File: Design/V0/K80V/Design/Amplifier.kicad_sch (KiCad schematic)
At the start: 59 parts

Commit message: affectations des empreintes
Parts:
- C1, C10, C11, C12, C13, C14, C15, C16, C2, C3, C4, C5, C6, C9: renamed from C?; footprint Design:C_0805_2012Metric -> Capacitor_SMD:C_0805_2012Metric
- C7, C8: renamed from C?; footprint Design:C_1210_3225Metric -> Capacitor_SMD:C_1210_3225Metric
- R1, R10, R12, R13, R14, R15, R16, R17, R18, R19, R2, R3, R4, R5, R6, R7, R8: renamed from R?; footprint Design:R_MELF_MMB-0207 -> Resistor_SMD:R_MELF_MMB-0207
- R11, R20, R21, R22, R23, R24, R25, R9: renamed from R?; footprint Design:R_0805_2012Metric -> Resistor_SMD:R_0805_2012Metric
- U1, U2, U4: renamed from U?; footprint Design:SOIC-8_3.9x4.9mm_P1.27mm -> Package_SO:SOIC-8_3.9x4.9mm_P1.27mm
- U3: renamed from U?; footprint Design:SOT-23 -> Package_SO:TSOP-6_1.65x3.05mm_P0.95mm
- U5: renamed from U?; footprint (none) -> Package_SO:SOIC-8_3.9x4.9mm_P1.27mm
- U6: renamed from U?; footprint Design:AD5752AREZ -> baclet_composants_np:AD5752AREZ
- U7: renamed from U?; footprint Design:MSOP-8_3x3mm_P0.65mm -> Package_SO:MSOP-8_3x3mm_P0.65mm
- U8: renamed from U?; footprint Design:TSSOP-14_4.4x5mm_P0.65mm -> Package_SO:TSSOP-14_4.4x5mm_P0.65mm
- gave numbers to parts that had none: 2

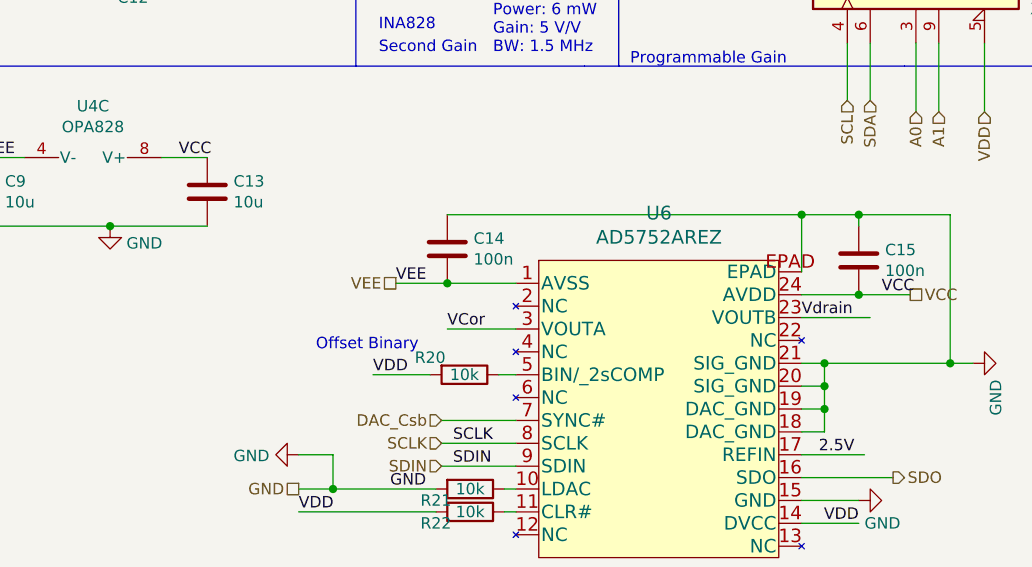
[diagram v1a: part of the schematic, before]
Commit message: Assignation des bons symboles
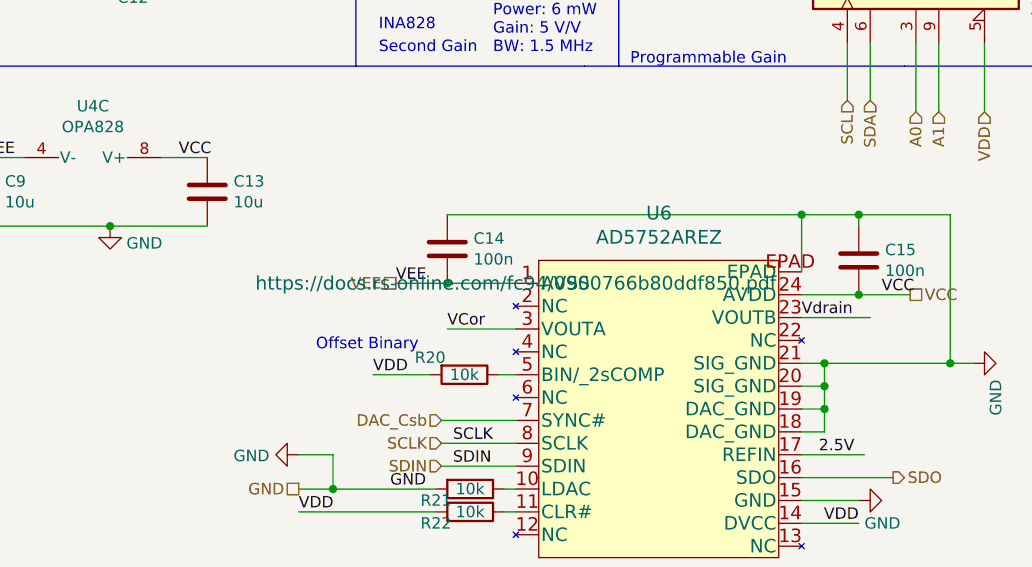
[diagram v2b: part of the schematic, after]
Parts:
- C1, C10, C11, C12, C13, C16, C2, C3, C4, C5, C6, C7, C8, C9: symbol Library:Device_C -> Device:C
- C14, C15: symbol archive:Device_C -> Device:C
- FET1: symbol 0_Composants:JFE2140 -> composants:JFE2140
- Q1: symbol Library:Transistor_BJT_BC850 -> Transistor_BJT:BC850
- R1, R10, R12, R13, R14, R15, R16, R17, R18, R19, R2, R3, R4, R5, R6, R7, R8: symbol Library:Device_R -> Device:R
- R11, R20, R21, R22, R23, R24, R25, R9: symbol archive:Device_R -> Device:R
- U1, U2, U4: symbol Library:Amplifier_Operational_AD8620 -> Amplifier_Operational:AD8620
- U3: footprint Package_SO:TSOP-6_1.65x3.05mm_P0.95mm -> Package_TO_SOT_SMD:SOT-23; symbol archive:REF3025 -> Reference_Voltage:REF3025
- U6: footprint baclet_composants_np:AD5752AREZ -> RE_24_ADI; symbol archive:David_Composants_AD5752AREZ -> composants:AD5752AREZ
- U7: symbol archive:Amplifier_Operational_ADA4807-2ARM -> Amplifier_Operational:ADA4807-2ARM
- U8: symbol archive:Potentiometer_Digital_X9118 -> Potentiometer_Digital:X9118
